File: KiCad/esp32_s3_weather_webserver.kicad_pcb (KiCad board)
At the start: 4 copper layers, 138 parts, among them IC301 CP2102N-A02-GQFN28R, IC401 ESP32-S3-WROOM-1-N16R8, IC501 VEML7700-TT, IC502 DS3231MZ+TRL, J201 Barrel_Jack_Switch_Pin3Ring, J301 USB_C_Receptacle_USB2.0, J302 USB_C_Receptacle_USB2.0, J401 Conn_01x04_Pin, J403 Conn_01x04_Pin, J404 TF-01A, Q401 SS8050, Q402 SS8050, U201 AMS1117-3.3, U202 TLV62569DBV, U203 HT7533-1, U301 USBLC6-2SC6, U302 USBLC6-2SC6, U501 BME280, U502 DS18B20, U503 LM35-LP, U504 DHT11

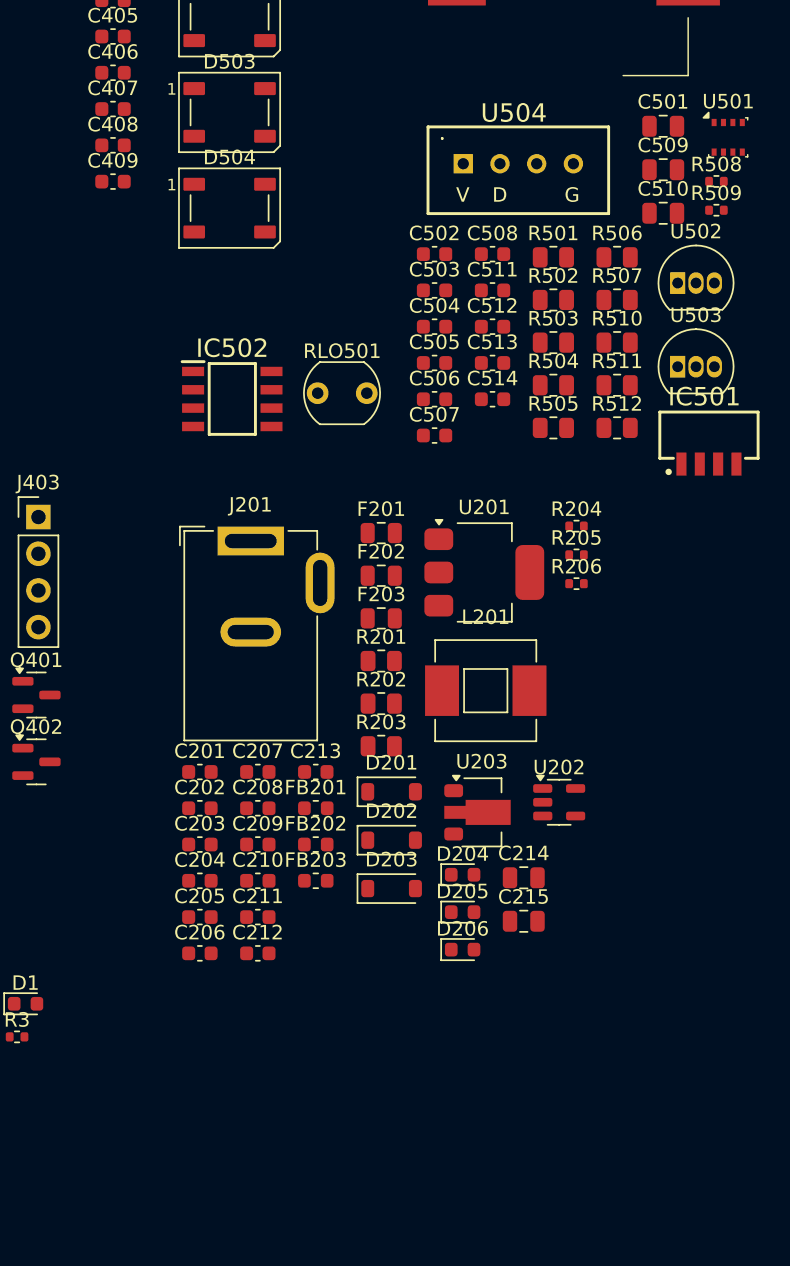
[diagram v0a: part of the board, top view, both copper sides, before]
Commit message: Add multisensor wrapper
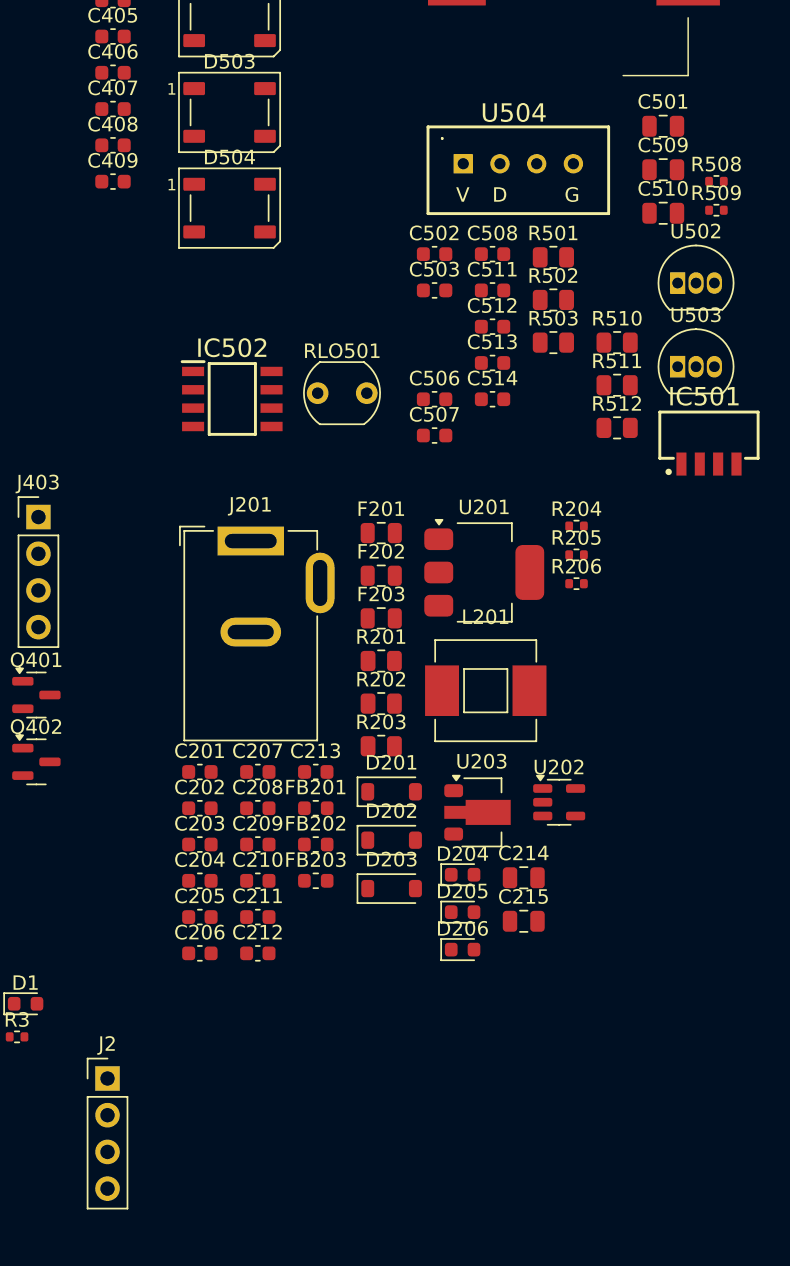
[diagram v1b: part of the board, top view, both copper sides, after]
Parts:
- removed C504: 100nF, Capacitor_SMD:C_0603_1608Metric
- removed C505: 10uF, Capacitor_SMD:C_0603_1608Metric
- removed R504, R505: 10kR, Resistor_SMD:R_0805_2012Metric
- removed R506, R507: 5k1R, Resistor_SMD:R_0805_2012Metric
- removed U501: BME280, Package_LGA:Bosch_LGA-8_2.5x2.5mm_P0.65mm_ClockwisePinNumbering
- added J2: Conn_01x04_Pin, Connector_PinHeader_2.54mm:PinHeader_1x04_P2.54mm_Vertical, F.Cu at (105.8, 109.4)
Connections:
- net GPIO14 renamed ENS160_INT
- BT501 pad 2: USR_BTN -> GND
- C1 pad 1: USR_BTN -> USR_BTN_LEFT
- C1 pad 2: USR_BTN -> GND
- C2 pad 1: USR_BTN -> USR_BTN_RIGHT
- C2 pad 2: USR_BTN -> GND
- C201 pad 2: USR_BTN -> GND
- C202 pad 2: USR_BTN -> GND
- C203 pad 2: USR_BTN -> GND
- C204 pad 2: USR_BTN -> GND
- C205 pad 2: USR_BTN -> GND
- C206 pad 2: USR_BTN -> GND
- C207 pad 2: USR_BTN -> GND
- C208 pad 2: USR_BTN -> GND
- C210 pad 2: USR_BTN -> GND
- C211 pad 2: USR_BTN -> GND
- C212 pad 2: USR_BTN -> GND
- C213 pad 2: USR_BTN -> GND
- C214 pad 2: USR_BTN -> GND
- C215 pad 2: USR_BTN -> GND
- C301 pad 2: USR_BTN -> GND
- C302 pad 2: USR_BTN -> GND
- C303 pad 2: USR_BTN -> GND
- C304 pad 2: USR_BTN -> GND
- C305 pad 2: USR_BTN -> GND
- C401 pad 2: USR_BTN -> GND
- C402 pad 2: USR_BTN -> GND
- C403 pad 2: USR_BTN -> GND
- C404 pad 2: USR_BTN -> GND
- C405 pad 2: USR_BTN -> GND
- C406 pad 2: USR_BTN -> GND
- C407 pad 2: USR_BTN -> GND
- C408 pad 2: USR_BTN -> GND
- C409 pad 2: USR_BTN -> GND
- C501 pad 2: USR_BTN -> GND
- C502 pad 2: USR_BTN -> GND
- C503 pad 2: USR_BTN -> GND
- C506 pad 2: USR_BTN -> GND
- C507 pad 2: USR_BTN -> GND
- C508 pad 2: USR_BTN -> GND
- C509 pad 2: USR_BTN -> GND
- C510 pad 2: USR_BTN -> GND
- C511 pad 2: USR_BTN -> GND
- C512 pad 2: USR_BTN -> GND
- C513 pad 1: +5V -> +3V3_PER
- C513 pad 2: USR_BTN -> GND
- C514 pad 1: +5V -> +3V3_PER
- C514 pad 2: USR_BTN -> GND
- D1 pad 1: USR_BTN -> GND
- D204 pad 1: USR_BTN -> GND
- D205 pad 1: USR_BTN -> GND
- D206 pad 1: USR_BTN -> GND
- D401 pad 2: USR_BTN -> GND
- D402 pad 2: USR_BTN -> GND
- D403 pad 2: USR_BTN -> GND
- D404 pad 2: USR_BTN -> GND
- D501 pad 3: USR_BTN -> GND
- D502 pad 3: USR_BTN -> GND
- D503 pad 3: USR_BTN -> GND
- D504 pad 3: USR_BTN -> GND
- IC301 pad 29: USR_BTN -> GND
- IC301 pad 3: USR_BTN -> GND
- IC401 pad 1: USR_BTN -> GND
- IC401 pad 10: USR_BTN -> USR_BTN_LEFT
- IC401 pad 11: USR_BTN -> USR_BTN_RIGHT
- IC401 pad 40: USR_BTN -> GND
- IC401 pad 41: USR_BTN -> GND
- IC501 pad 3: USR_BTN -> GND
- IC502 pad 5: USR_BTN -> GND
- J201 pad 2: USR_BTN -> GND
- J201 pad 3: USR_BTN -> GND
- J301 pad A1: USR_BTN -> GND
- J301 pad A12: USR_BTN -> GND
- J301 pad B1: USR_BTN -> GND
- J301 pad B12: USR_BTN -> GND
- J302 pad A1: USR_BTN -> GND
- J302 pad A12: USR_BTN -> GND
- J302 pad B1: USR_BTN -> GND
- J302 pad B12: USR_BTN -> GND
- J401 pad 1: USR_BTN -> GND
- J403 pad 1: USR_BTN -> GND
- J404 pad 6: USR_BTN -> GND
- J404 pad MP1: USR_BTN -> GND
- J404 pad MP2: USR_BTN -> GND
- J404 pad MP3: USR_BTN -> GND
- J404 pad MP4: USR_BTN -> GND
- R1 pad 1: +3V3 -> GND
- R1 pad 2: Net-(R1-Pad2) -> USR_BTN_LEFT
- R2 pad 1: +3V3 -> GND
- R2 pad 2: Net-(R2-Pad2) -> USR_BTN_RIGHT
- R202 pad 1: USR_BTN -> GND
- R303 pad 2: USR_BTN -> GND
- R304 pad 2: USR_BTN -> GND
- R305 pad 2: USR_BTN -> GND
- R306 pad 2: USR_BTN -> GND
- R307 pad 2: USR_BTN -> GND
- R308 pad 2: USR_BTN -> GND
- R409 pad 1: +3V3 -> GND
- R409 pad 2: Net-(R409-Pad2) -> USR_BTN
- R501 pad 2: USR_BTN -> GND
- R509 pad 1: +5V -> +3V3_PER
- SW1 pad 1: Net-(R1-Pad2) -> +3V3
- SW1 pad 2: USR_BTN -> USR_BTN_LEFT
- SW1 pad 3: USR_BTN -> USR_BTN_LEFT
- SW1 pad 4: Net-(R1-Pad2) -> +3V3
- SW2 pad 1: Net-(R2-Pad2) -> +3V3
- SW2 pad 2: USR_BTN -> USR_BTN_RIGHT
- SW2 pad 3: USR_BTN -> USR_BTN_RIGHT
- SW2 pad 4: Net-(R2-Pad2) -> +3V3
- SW401 pad 2: USR_BTN -> GND
- SW401 pad 3: USR_BTN -> GND
- SW402 pad 2: USR_BTN -> GND
- SW402 pad 3: USR_BTN -> GND
- SW403 pad 1: Net-(R409-Pad2) -> +3V3
- SW403 pad 4: Net-(R409-Pad2) -> +3V3
- U201 pad 1: USR_BTN -> GND
- U202 pad 2: USR_BTN -> GND
- U203 pad 1: USR_BTN -> GND
- U301 pad 2: USR_BTN -> GND
- U302 pad 2: USR_BTN -> GND
- U502 pad 1: USR_BTN -> GND
- U503 pad 3: USR_BTN -> GND
- U504 pad 1: +5V -> +3V3_PER
- U504 pad 4: USR_BTN -> GND

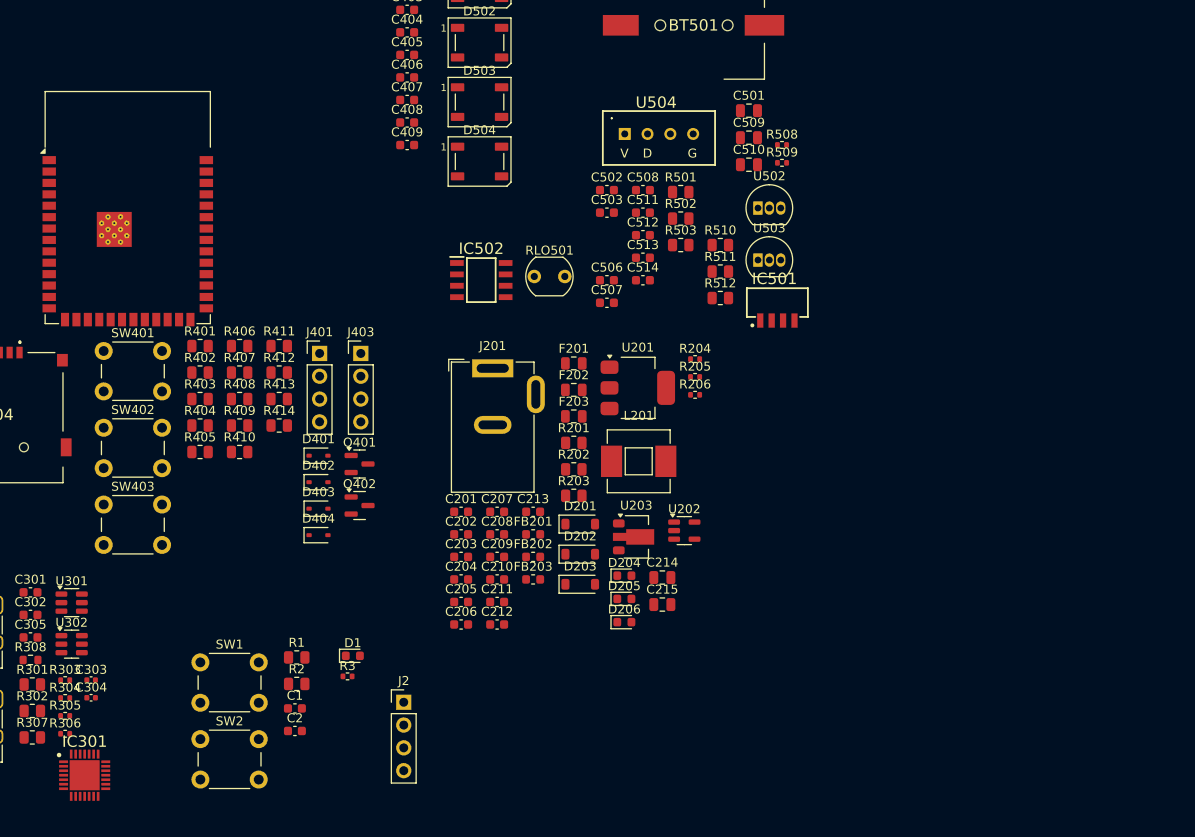
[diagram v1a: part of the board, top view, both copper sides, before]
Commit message: Add sensor footprints
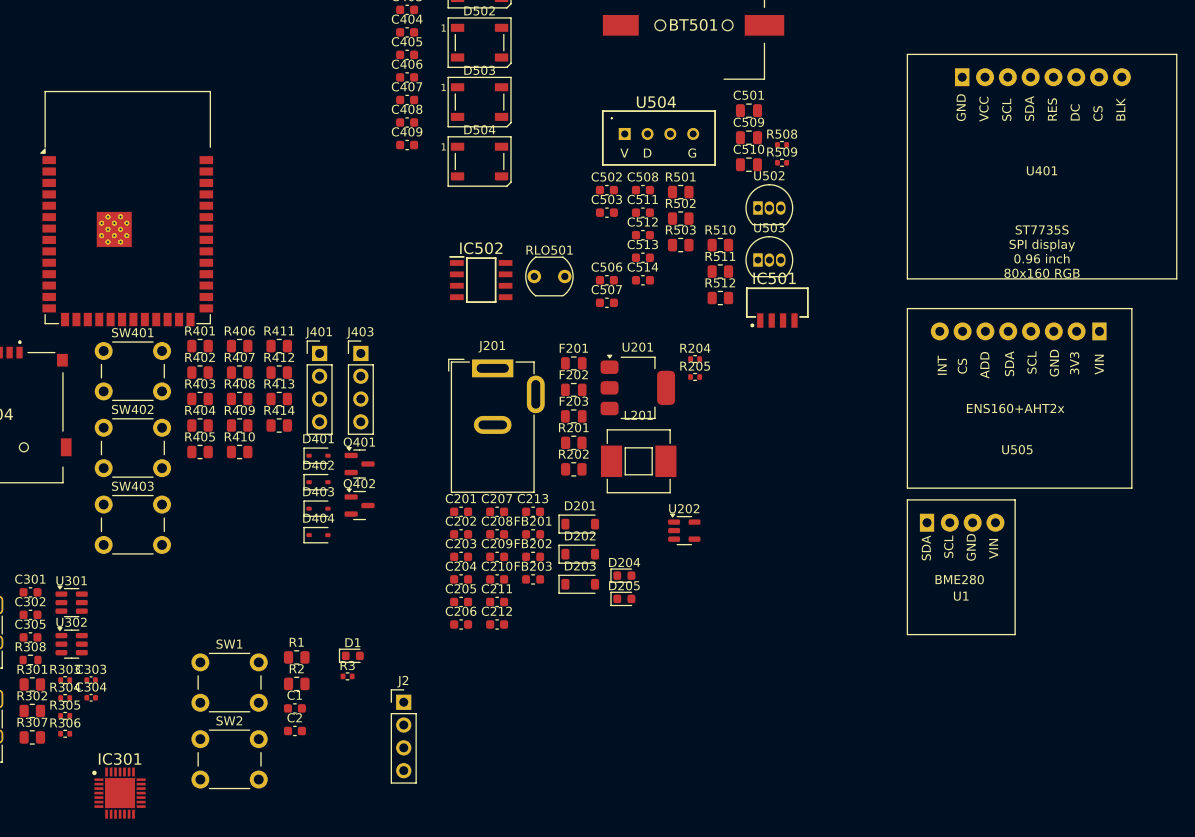
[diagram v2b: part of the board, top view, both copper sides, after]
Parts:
- removed C214, C215: 22uF, Capacitor_SMD:C_0805_2012Metric
- removed D206: LED, LED_SMD:LED_0603_1608Metric
- removed R203: 10R, Resistor_SMD:R_0805_2012Metric
- removed R206: 510R, Resistor_SMD:R_0402_1005Metric
- removed U203: HT7533-1, Package_TO_SOT_SMD:SOT-89-3
- added U1: ~, esp32_s3_weather_webserver:BME280, F.Cu at (161.8, 86.8)
- added U401: ~, esp32_s3_weather_webserver:ST7735S, F.Cu at (161.8, 37.2)
- added U505: ~, esp32_s3_weather_webserver:ENS160+AHT2x, F.Cu at (161.8, 65.5)
- moved IC301 4.41 mm to (74.2, 119.5)
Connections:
- C501 pad 1: +3V3A -> +3V3_PER
- C509 pad 1: +3.3VA -> +5V
- C510 pad 1: +3.3VA -> +5V
- R508 pad 1: +3.3VA -> +5V
- RLO501 pad 2: +3V3A -> +3V3_PER
- U502 pad 3: +3.3VA -> +5V
- U503 pad 1: +3.3VA -> +5V

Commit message: BOM updates
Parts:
- added H1: MountingHole, MountingHole:MountingHole_3.2mm_M3, F.Cu at (31.0, 107.4)
- added H2: MountingHole, MountingHole:MountingHole_3.2mm_M3, F.Cu at (31.0, 115.3)
- added H3: MountingHole, MountingHole:MountingHole_3.2mm_M3, F.Cu at (31.0, 123.3)
- added H4: MountingHole, MountingHole:MountingHole_3.2mm_M3, F.Cu at (31.0, 131.2)
- added J1: Conn_01x08_Pin, Connector_PinHeader_2.54mm:PinHeader_1x08_P2.54mm_Vertical, F.Cu at (215.5, 42.0)
- C303, C304: footprint Capacitor_SMD:C_0402_1005Metric -> Capacitor_SMD:C_0603_1608Metric
- C501, C509, C510: footprint Capacitor_SMD:C_0805_2012Metric -> Capacitor_SMD:C_0603_1608Metric
- R204, R205, R3, R303, R304, R305, R306, R508, R509: footprint Resistor_SMD:R_0402_1005Metric -> Resistor_SMD:R_0805_2012Metric
- R308: footprint Resistor_SMD:R_0603_1608Metric -> Resistor_SMD:R_0805_2012Metric
- moved F201 145.3 mm to (30.5, 182.2), turned to 90 degrees
- moved F203 130.3 mm to (45.7, 181.2), turned to -90 degrees
- moved J201 125.3 mm to (36.9, 169.7)
- moved F202 122.4 mm to (64.5, 181.1), turned to -90 degrees
- moved D203 118.2 mm to (23.8, 156.6), turned to -90 degrees
- moved U201 118.1 mm to (89.7, 184.7)
- moved C213 115.7 mm to (26.3, 155.8), turned to 90 degrees
- moved D202 113.3 mm to (31.8, 156.6), turned to -90 degrees
- moved FB203 112.0 mm to (27.3, 158.3)
- moved D201 108.7 mm to (39.8, 156.6), turned to -90 degrees
- moved FB202 106.9 mm to (35.2, 158.2)
- moved C212 103.7 mm to (28.3, 155.8), turned to 90 degrees
- moved FB201 102.4 mm to (43.1, 158.1)
- moved C211 100.1 mm to (34.2, 155.7), turned to 90 degrees
- moved C202 100.0 mm to (84.2, 186.7), turned to -90 degrees
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
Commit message: BOM updates. First layout
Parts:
- removed C1, C2, C409, C514: 100nF, Capacitor_SMD:C_0603_1608Metric
- removed D1: LED, LED_SMD:LED_0603_1608Metric
- removed D501, D502, D503, D504: WS2812B, LED_SMD:LED_WS2812B_PLCC4_5.0x5.0mm_P3.2mm
- removed H1, H2, H3, H4: MountingHole, MountingHole:MountingHole_3.2mm_M3
- removed J1: Conn_01x08_Pin, Connector_PinHeader_2.54mm:PinHeader_1x08_P2.54mm_Vertical
- removed J2: Conn_01x04_Pin, Connector_PinHeader_2.54mm:PinHeader_1x04_P2.54mm_Vertical
- removed R1, R2, R414, R511: 10kR, Resistor_SMD:R_0805_2012Metric
- removed R3: 510R, Resistor_SMD:R_0805_2012Metric
- removed R512: 0R, Resistor_SMD:R_0805_2012Metric
- removed SW1, SW2, SW403: ~, esp32_s3_weather_webserver:SW_PUSH_6mm_H5mm
- removed U1: ~, esp32_s3_weather_webserver:BME280
- added C504: 100nF, Capacitor_SMD:C_0402_1005Metric, F.Cu at (94.8, 87.2)
- added C505: 10uF, Capacitor_SMD:C_0603_1608Metric, F.Cu at (36.0, 62.4)
- added D206: WS2812B, LED_SMD:LED_WS2812B_PLCC4_5.0x5.0mm_P3.2mm, F.Cu at (213.9, 102.7)
- added D207: WS2812B, LED_SMD:LED_WS2812B_PLCC4_5.0x5.0mm_P3.2mm, F.Cu at (214.4, 108.7)
- added D208: LED, LED_SMD:LED_0603_1608Metric, F.Cu at (235.2, 93.1)
- added D209: LED, LED_SMD:LED_0603_1608Metric, F.Cu at (235.2, 95.7)
- added D210: LED, LED_SMD:LED_0603_1608Metric, F.Cu at (235.2, 98.3)
- added H101: MountingHole, MountingHole:MountingHole_3.2mm_M3, F.Cu at (217.6, 36.6)
- added H102: MountingHole, MountingHole:MountingHole_3.2mm_M3, F.Cu at (217.6, 44.6)
- added H103: MountingHole, MountingHole:MountingHole_3.2mm_M3, F.Cu at (217.6, 52.5)
- added H104: MountingHole, MountingHole:MountingHole_3.2mm_M3, F.Cu at (217.6, 60.5)
- added J402: Conn_01x04_Pin, Connector_PinHeader_2.54mm:PinHeader_1x04_P2.54mm_Vertical, F.Cu at (18.2, 35.4)
- added J405: Conn_01x08_Pin, Connector_PinHeader_2.54mm:PinHeader_1x08_P2.54mm_Vertical, F.Cu at (251.8, 35.0)
- added R203: 0R, Resistor_SMD:R_0805_2012Metric, F.Cu at (211.5, 84.5)
- added R206: 510R, Resistor_SMD:R_0402_1005Metric, F.Cu at (238.2, 98.3)
- added R504: 5k1R, Resistor_SMD:R_0402_1005Metric, F.Cu at (36.0, 55.9)
- added R505: 5k1R, Resistor_SMD:R_0402_1005Metric, F.Cu at (36.6, 66.4)
- added R506: 10kR, Resistor_SMD:R_0402_1005Metric, F.Cu at (143.4, 74.3)
- added R507: 10kR, Resistor_SMD:R_0402_1005Metric, F.Cu at (141.4, 74.3)
- added SW501: ~, esp32_s3_weather_webserver:SW_PUSH_6mm_H5mm, F.Cu at (103.2, 102.8)
- added SW502: ~, esp32_s3_weather_webserver:SW_PUSH_6mm_H5mm, F.Cu at (116.7, 102.2)
- added SW503: ~, esp32_s3_weather_webserver:SW_PUSH_6mm_H5mm, F.Cu at (129.7, 102.2)
- added U501: ~, esp32_s3_weather_webserver:BME280, F.Cu at (133.6, 83.7)
- C202, C203, C302, C303, C304, C403, C404, C405, C406, C408, C508, C512: footprint Capacitor_SMD:C_0603_1608Metric -> Capacitor_SMD:C_0402_1005Metric
- C502, C510, C511, C513: value 10uF -> 100nF; footprint Capacitor_SMD:C_0603_1608Metric -> Capacitor_SMD:C_0402_1005Metric
- C503, C506: value 100nF -> 10uF
- D204, D205: value LED -> WS2812B; footprint LED_SMD:LED_0603_1608Metric -> LED_SMD:LED_WS2812B_PLCC4_5.0x5.0mm_P3.2mm
- R201, R202, R204, R205, R301, R302, R303, R304, R305, R306, R307, R404, R406, R407, R409, R410, R411, R412, R413, R501, R502, R503, R510: footprint Resistor_SMD:R_0805_2012Metric -> Resistor_SMD:R_0402_1005Metric
- R308: footprint Resistor_SMD:R_0805_2012Metric -> Resistor_SMD:R_0603_1608Metric
- R508, R509: value 5k1R -> 10kR; footprint Resistor_SMD:R_0805_2012Metric -> Resistor_SMD:R_0402_1005Metric
- moved U202 120.0 mm to (58.0, 79.8), turned to -90 degrees
- moved L201 114.3 mm to (52.0, 80.0), turned to 90 degrees
- moved C208 112.8 mm to (58.0, 76.2)
- moved C510 111.1 mm to (34.4, 66.4), turned to 180 degrees
- moved C509 110.9 mm to (34.9, 64.9), turned to 180 degrees
- moved C209 110.6 mm to (62.2, 79.2), turned to -90 degrees
- moved U502 110.6 mm to (34.7, 59.4)
- moved R202 105.1 mm to (60.8, 81.0), turned to 90 degrees
- moved C501 104.8 mm to (39.7, 52.1), turned to -90 degrees
- moved R501 104.6 mm to (32.0, 50.6), turned to 90 degrees
- moved R201 104.5 mm to (60.8, 78.7), turned to 90 degrees
- moved C207 104.3 mm to (58.0, 83.2)
- moved U503 104.2 mm to (41.0, 59.2)
- moved R205 102.5 mm to (238.2, 95.7)
- moved R204 102.3 mm to (238.1, 93.0)
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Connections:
- C502 pad 1: +3V3_PER -> LDR
- C506 pad 1: LDR -> +5V
- C509 pad 1: +5V -> +3V3_PER
- C510 pad 1: +5V -> +3V3_PER
- C511 pad 1: +3V3_PER -> USR_BTN
- C512 pad 1: +3V3_PER -> USR_BTN_LEFT
- C513 pad 1: +3V3_PER -> USR_BTN_RIGHT
- D204 pad 1: GND -> +5V
- D204 pad 2: /[2] Power/LED_3V3_A -> Net-(D204-DOUT)
- D205 pad 1: GND -> +5V
- D205 pad 2: /[2] Power/LED_3V3_PER_A -> Net-(D205-DOUT)
- R409 pad 1: GND -> FSPI_MISO
- R409 pad 2: USR_BTN -> +3V3_PER
- R410 pad 1: FSPI_MISO -> FSPI_MOSI
- R411 pad 1: FSPI_MOSI -> FSPI_SCK
- R412 pad 1: FSPI_SCK -> FSPI_SS
- R413 pad 1: FSPI_SS -> SD_CD
- R508 pad 1: +5V -> GND
- R508 pad 2: DS18B20 -> USR_BTN
- R509 pad 1: +3V3_PER -> GND
- R509 pad 2: DHT11 -> USR_BTN_LEFT
- R510 pad 1: I2C_SDA -> GND
- R510 pad 2: +3V3_PER -> USR_BTN_RIGHT

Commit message: Layout updates
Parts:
- BT501: moved to B.Cu
- moved R204 175.2 mm to (63.1, 84.9), turned to -90 degrees
- moved R205 173.5 mm to (65.0, 85.0), turned to -90 degrees
- moved D208 172.5 mm to (63.0, 82.0), turned to -90 degrees
- moved R206 171.7 mm to (67.0, 85.0), turned to -90 degrees
- moved H104 171.5 mm to (52.2, 106.0)
- moved D209 170.7 mm to (65.0, 82.0), turned to -90 degrees
- moved D210 168.9 mm to (67.0, 82.0), turned to -90 degrees
- moved H101 166.2 mm to (52.5, 55.5)
- moved J405 111.8 mm to (148.0, 76.6)
- moved H103 89.5 mm to (146.2, 106.5)
- moved C510 77.9 mm to (112.0, 60.0), turned to 0 degrees
- moved D204 77.2 mm to (136.9, 79.7)
- moved D205 77.2 mm to (137.1, 86.2)
- moved R203 77.2 mm to (135.0, 74.5)
- moved D206 77.1 mm to (137.5, 92.5)
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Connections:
- SW501 pad 1: +3V3 -> +3V3_PER
- SW501 pad 4: +3V3 -> +3V3_PER
- SW502 pad 1: +3V3 -> +3V3_PER
- SW502 pad 4: +3V3 -> +3V3_PER
- SW503 pad 1: +3V3 -> +3V3_PER
- SW503 pad 4: +3V3 -> +3V3_PER
